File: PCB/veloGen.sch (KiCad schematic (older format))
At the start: 18 parts

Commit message: Got more specific about parts
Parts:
- D? (x4): value D_Schottky -> B5819WS
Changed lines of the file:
@@
 LIBS:valves
 LIBS:myStuff
+LIBS:veloGen-cache
 EELAYER 26 0
 EELAYER END
@@
 P 2000 1350
 F 0 "D?" V 2000 1429 50  0000 L CNN
-F 1 "D_Schottky" V 2045 1429 50  0001 L CNN
+F 1 "B5819WS" V 2045 1429 50  0001 L CNN
 F 2 "" H 2000 1350 50  0001 C CNN
 F 3 "" H 2000 1350 50  0001 C CNN
@@
 P 2600 1350
 F 0 "D?" V 2600 1429 50  0000 L CNN
-F 1 "D_Schottky" V 2645 1429 50  0001 L CNN
+F 1 "B5819WS" V 2645 1429 50  0001 L CNN
 F 2 "" H 2600 1350 50  0001 C CNN
 F 3 "" H 2600 1350 50  0001 C CNN
@@
 P 2000 2000
 F 0 "D?" V 2000 2079 50  0000 L CNN
-F 1 "D_Schottky" V 2045 2079 50  0001 L CNN
+F 1 "B5819WS" V 2045 2079 50  0001 L CNN
 F 2 "" H 2000 2000 50  0001 C CNN
 F 3 "" H 2000 2000 50  0001 C CNN
@@
 P 2600 2000
 F 0 "D?" V 2600 2079 50  0000 L CNN
-F 1 "D_Schottky" V 2645 2079 50  0001 L CNN
+F 1 "B5819WS" V 2645 2079 50  0001 L CNN
 F 2 "" H 2600 2000 50  0001 C CNN
 F 3 "" H 2600 2000 50  0001 C CNN

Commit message: Started the Schematic
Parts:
- removed Q?: FDS9934C, Housings_SOIC:SOIC-8_3.9x4.9mm_Pitch1.27mm, symbol FDS9934C
- removed Q?: BSS138, TO_SOT_Packages_SMD:SOT-23, symbol BSS138
- removed R?: R, symbol R
- removed U?: esp8266_esp-02, symbol esp8266_esp-02
- added C? (x5): 470n, symbol C
- added C? (x4): 47n, symbol C
- added D?: B5819WS, symbol D_Schottky
- added P?: TTL_232R_3V3, Pin_Headers:Pin_Header_Straight_1x06_Pitch2.54mm, symbol TTL_232R_3V3
- added Q?: STL6N3LLH6, myStuff:PowerFLAT_2x2, symbol STL6N3LLH6
- added R?: 47k, symbol R
- added R? (x4): R, symbol R
- added U?: LTC4440-5, TO_SOT_Packages_SMD:SOT-23-6_Handsoldering, symbol LTC4440
- added U? (x2): TS1101, TO_SOT_Packages_SMD:SOT-23-6_Handsoldering, symbol TS1101
- added U?: ESP-WROOM-32, myStuff:ESP-WROOM-32, symbol ESP-WROOM-32
- C?: value 1u -> 470n
- D?: value D_Schottky -> STPS3L40UF; footprint (none) -> Diodes_SMD:D_SMB_Standard
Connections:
- net labels added: +BATT, Ibatt, IbattSign, Igen, Vbatt, Vgen, buckPwm, speedPulse
- wire segments 45 -> 149
- no-connect marks 1 -> 2
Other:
- note added: "A minimalistic bluetooth bike computer\nand hub dynamo power manager"
- note added: "TODO:\n* Voltage divider values\n* Current Shunt values\n* ESP32 Pin assignment"
- moved on the sheet: C?, D?, J?, L?, R?, U?

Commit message: Refined the schematic
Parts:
- removed C? (x2): 10u, symbol C
- removed C? (x2): 470n, symbol C
- removed D?: STPS3L40UF, Diodes_SMD:D_SMB_Standard, symbol D_Schottky
- removed D?: B5819WS, symbol D_Schottky
- removed L?: L, symbol L
- removed Q?: STL6N3LLH6, myStuff:PowerFLAT_2x2, symbol STL6N3LLH6
- removed U?: LTC4440-5, TO_SOT_Packages_SMD:SOT-23-6_Handsoldering, symbol LTC4440
- added P?: CONN_01X04, symbol CONN_01X04
- added Q?: IRF7324, Housings_SOIC:SOIC-8_3.9x4.9mm_Pitch1.27mm, symbol IRF7324
- added Q?: 2N7002, TO_SOT_Packages_SMD:SOT-23, symbol 2N7002
- added R? (x2): 200R, symbol R
- added R? (x2): 4k7, symbol R
- added R?: 4.7Meg, symbol R
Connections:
- net labels added: extScl, extSda, vExtEnable
- wire segments 149 -> 102
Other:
- moved on the sheet: C?, U?

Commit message: Schematic one step closer
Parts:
- removed Q?: IRF7324, Housings_SOIC:SOIC-8_3.9x4.9mm_Pitch1.27mm, symbol IRF7324
- removed Q?: 2N7002, TO_SOT_Packages_SMD:SOT-23, symbol 2N7002
- added J1: CONN_01X02, Pin_Headers:Pin_Header_Straight_1x02_Pitch1.27mm, symbol CONN_01X02
- added Q1: STL4P3LLH6, myStuff:PowerFLAT_2x2, symbol STL4P3LLH6
- added Q2: BSS138_ok, TO_SOT_Packages_SMD:SOT-23, symbol BSS138_ok
- added R2: 470k, Resistors_SMD:R_0805, symbol R
- C1, C2, C3, C4, C5, C6, C7, C8: renamed from C?; footprint (none) -> Capacitors_SMD:C_0805
- D1, D2, D3, D4: renamed from D?; footprint (none) -> Diodes_SMD:D_SOD-323
- J2, J3: renamed from J?; footprint (none) -> Pin_Headers:Pin_Header_Straight_1x02_Pitch1.27mm
- P2: renamed from P?; footprint (none) -> Pin_Headers:Pin_Header_Straight_1x04_Pitch1.27mm
- R1, R10, R11, R12, R13, R3, R8, R9: renamed from R?; footprint (none) -> Resistors_SMD:R_0805
- R4: renamed from R?; value R -> 30k1; footprint (none) -> Resistors_SMD:R_0805
- R5: renamed from R?; value R -> 1k15; footprint (none) -> Resistors_SMD:R_0805
- R6: renamed from R?; value R -> 1M150; footprint (none) -> Resistors_SMD:R_0805
- R7: renamed from R?; value R -> 365k; footprint (none) -> Resistors_SMD:R_0805
- gave numbers to parts that had none: 5
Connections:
- net labels added: rstBtn
- wire segments 102 -> 114
- no-connect marks 2 -> 23
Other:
- note added: "30 V --> 1.1 V"
- note removed: "TODO:\n* Voltage divider values\n* Current Shunt values\n* ESP32 Pin assignment"
- moved on the sheet: C1, P1, U1

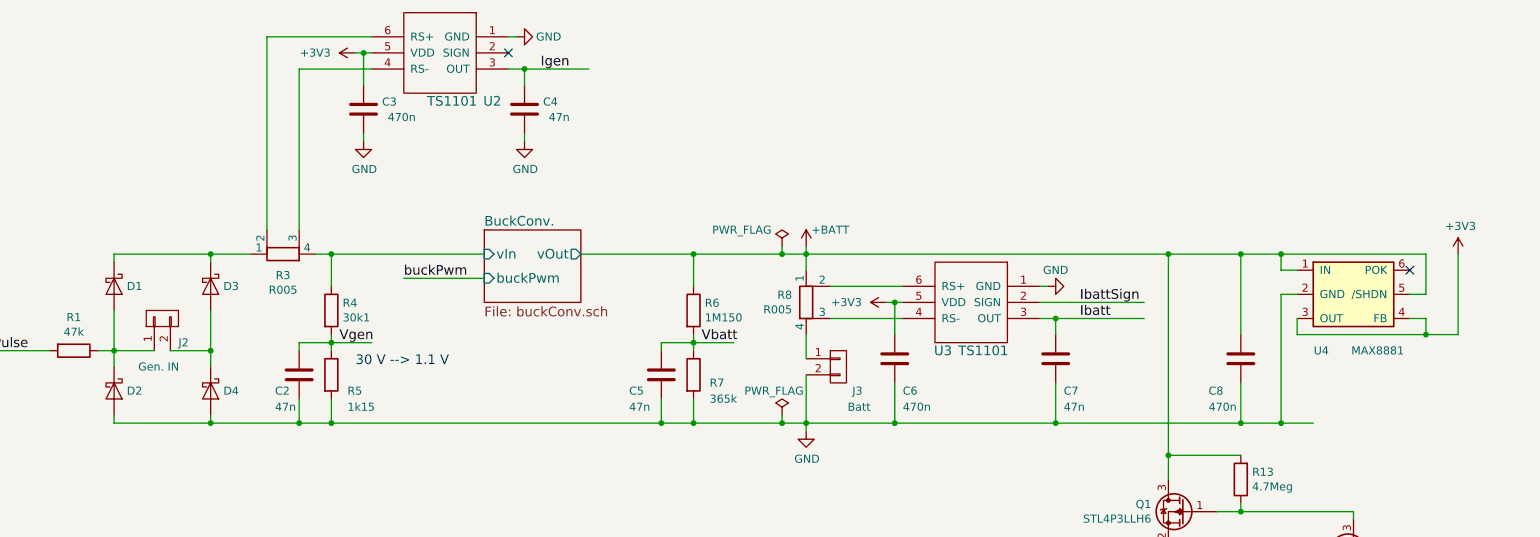
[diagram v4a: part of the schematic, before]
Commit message: Moved around some components a bit
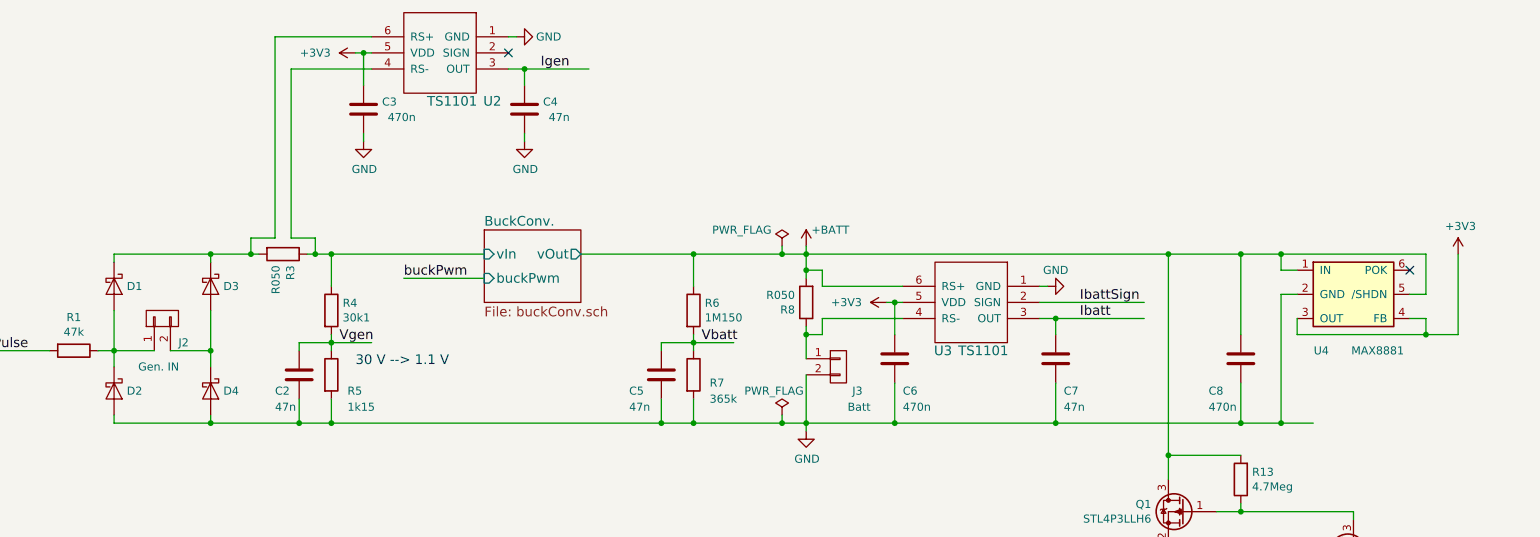
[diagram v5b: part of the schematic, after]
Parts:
- removed R3, R8: R005, Resistors_SMD:R_0805, symbol R_Shunt
- added R3, R8: R050, Resistors_SMD:R_0805, symbol R
- J1, J2, J3: footprint Pin_Headers:Pin_Header_Straight_1x02_Pitch1.27mm -> Pin_Headers:Pin_Header_Straight_1x02_Pitch2.54mm
- P2: footprint Pin_Headers:Pin_Header_Straight_1x04_Pitch1.27mm -> Pin_Headers:Pin_Header_Straight_1x04_Pitch2.54mm
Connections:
- wire segments 114 -> 121
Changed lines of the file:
@@
 F 0 "J2" V 2400 2800 50  0000 R CNN
 F 1 "Gen. IN" V 2250 3050 50  0000 R CNN
-F 2 "Pin_Headers:Pin_Header_Straight_1x02_Pitch1.27mm" H 2550 2900 50  0001 C CNN
+F 2 "Pin_Headers:Pin_Header_Straight_1x02_Pitch2.54mm" H 2550 2900 50  0001 C CNN
 F 3 "" H 2550 2900 50  0001 C CNN
 	1    2550 2900
@@
 $EndComp
 $Comp
-L R_Shunt R3
-U 1 1 58CDA790
-P 3300 2500
-F 0 "R3" V 3168 2500 50  0000 C CNN
-F 1 "R005" V 3077 2500 50  0000 C CNN
-F 2 "Resistors_SMD:R_0805" V 3230 2500 50  0001 C CNN
-F 3 "" H 3300 2500 50  0001 C CNN
-	1    3300 2500
-	0    -1   -1   0
-$EndComp
-$Comp
 L CONN_01X02 J3
 U 1 1 58CDC990
@@
 F 0 "J3" H 6900 3050 50  0000 R CNN
 F 1 "Batt" H 6950 2950 50  0000 R CNN
-F 2 "Pin_Headers:Pin_Header_Straight_1x02_Pitch1.27mm" H 6750 3200 50  0001 C CNN
+F 2 "Pin_Headers:Pin_Header_Straight_1x02_Pitch2.54mm" H 6750 3200 50  0001 C CNN
 F 3 "" H 6750 3200 50  0001 C CNN
 	1    6750 3200
-	1    0    0    -1
-$EndComp
-$Comp
-L R_Shunt R8
-U 1 1 58CDCDCD
-P 6550 2800
-F 0 "R8" H 6462 2846 50  0000 R CNN
-F 1 "R005" H 6462 2755 50  0000 R CNN
-F 2 "Resistors_SMD:R_0805" V 6480 2800 50  0001 C CNN
-F 3 "" H 6550 2800 50  0001 C CNN
-	1    6550 2800
 	1    0    0    -1
 $EndComp
@@
 F 0 "P2" H 8650 5100 50  0000 C CNN
 F 1 "CONN_01X04" H 8600 5000 50  0000 C CNN
-F 2 "Pin_Headers:Pin_Header_Straight_1x04_Pitch1.27mm" H 8500 5300 50  0001 C CNN
+F 2 "Pin_Headers:Pin_Header_Straight_1x04_Pitch2.54mm" H 8500 5300 50  0001 C CNN
 F 3 "" H 8500 5300 50  0000 C CNN
 	1    8500 5300
@@
 F 0 "J1" H 1419 5075 50  0000 C CNN
 F 1 "CONN_01X02" H 1419 5166 50  0000 C CNN
-F 2 "Pin_Headers:Pin_Header_Straight_1x02_Pitch1.27mm" H 1500 5350 50  0001 C CNN
+F 2 "Pin_Headers:Pin_Header_Straight_1x02_Pitch2.54mm" H 1500 5350 50  0001 C CNN
 F 3 "" H 1500 5350 50  0001 C CNN
 	1    1500 5350
@@
 Connection ~ 6400 3550
 Wire Wire Line
-	6400 3500 6400 3550
+	6400 3550 6400 3500
 Connection ~ 6400 2500
 Wire Wire Line
@@
 	8750 5350 8700 5350
 Wire Wire Line
-	2250 2500 3100 2500
+	2250 2500 3150 2500
 Wire Wire Line
 	4900 5800 5550 5800
@@
 	8800 2500 8800 3900
 Wire Wire Line
-	10400 2750 10400 2500
+	10400 2500 10400 2750
 Connection ~ 9500 2500
 Wire Wire Line
@@
 	9600 2600 9500 2600
 Wire Wire Line
-	9500 2750 9500 3550
-Wire Wire Line
-	9600 2750 9500 2750
+	9500 3550 9500 2750
+Wire Wire Line
+	9500 2750 9600 2750
 Wire Wire Line
 	9600 2900 9600 3000
 Connection ~ 9250 3550
 Wire Wire Line
-	9250 3300 9250 3550
+	9250 3550 9250 3300
 Connection ~ 9500 3550
 Wire Wire Line
-	3500 2500 4550 2500
+	3450 2500 4550 2500
 Wire Wire Line
 	4050 2650 4550 2650
@@
 	8100 3000 8100 2900
 Wire Wire Line
-	3850 1350 3400 1350
-Wire Wire Line
-	3200 1150 3850 1150
+	3850 1350 3350 1350
+Wire Wire Line
+	3250 1150 3850 1150
 Connection ~ 4800 1350
 Wire Wire Line
@@
 Connection ~ 2950 5100
 Wire Wire Line
-	2950 5100 2950 5100
+	2900 5100 3000 5100
 Connection ~ 2550 5100
 Wire Wire Line
@@
 Wire Wire Line
 	2550 5200 3000 5200
-Wire Wire Line
-	2900 5100 3000 5100
 Wire Wire Line
 	2500 5100 2600 5100
 Connection ~ 5650 3550
 Wire Wire Line
-	5650 3400 5650 3550
+	5650 3550 5650 3400
 Connection ~ 5850 3550
 Wire Wire Line
-	5850 3400 5850 3550
+	5850 3550 5850 3400
 Connection ~ 5850 2500
 Wire Wire Line
@@
 Connection ~ 8100 3550
 Wire Wire Line
-	8100 3300 8100 3550
-Wire Wire Line
-	3200 2350 3200 1150
-Wire Wire Line
-	3400 1350 3400 2350
+	8100 3550 8100 3300
+Wire Wire Line
+	3250 1150 3250 2400
+Wire Wire Line
+	3350 1350 3350 2400
 Wire Wire Line
 	3800 1800 3800 1750
@@
 	7050 2800 7150 2800
 Wire Wire Line
-	7150 2900 6700 2900
-Wire Wire Line
-	7150 2700 6700 2700
+	6650 2900 7150 2900
+Wire Wire Line
+	6650 2700 7150 2700
 Wire Wire Line
 	9600 3000 10600 3000
@@
 	9250 3000 9250 2500
 Wire Wire Line
-	10300 2750 10400 2750
+	10400 2750 10300 2750
 Connection ~ 6550 3550
 Connection ~ 6550 2500
 Wire Wire Line
-	6550 2450 6550 2600
-Wire Wire Line
-	6550 3000 6550 3150
+	6550 2450 6550 2650
+Wire Wire Line
+	6550 2950 6550 3150
 Wire Wire Line
 	6550 3250 6550 3600
 Wire Wire Line
-	10400 2500 5150 2500
+	5150 2500 10400 2500
 Connection ~ 2850 3550
 Connection ~ 2850 2500
@@
 	1    0    0    -1
 $EndComp
+$Comp
+L R R3
+U 1 1 58D38E14
+P 3300 2500
+F 0 "R3" H 3370 2546 50  0000 L CNN
+F 1 "R050" H 3370 2455 50  0000 L CNN
+F 2 "Resistors_SMD:R_0805" V 3230 2500 50  0001 C CNN
+F 3 "" H 3300 2500 50  0001 C CNN
+	1    3300 2500
+	0    1    1    0
+$EndComp
+Wire Wire Line
+	3250 2400 3100 2400
+Wire Wire Line
+	3100 2400 3100 2500
+Connection ~ 3100 2500
+Wire Wire Line
+	3350 2400 3500 2400
+Wire Wire Line
+	3500 2400 3500 2500
+Connection ~ 3500 2500
+$Comp
+L R R8
+U 1 1 58D39C69
+P 6550 2800
+F 0 "R8" H 6620 2846 50  0000 L CNN
+F 1 "R050" H 6620 2755 50  0000 L CNN
+F 2 "Resistors_SMD:R_0805" V 6480 2800 50  0001 C CNN
+F 3 "" H 6550 2800 50  0001 C CNN
+	1    6550 2800
+	-1   0    0    1
+$EndComp
+Wire Wire Line
+	6650 2900 6650 3000
+Wire Wire Line
+	6650 3000 6550 3000
+Connection ~ 6550 3000
+Wire Wire Line
+	6650 2700 6650 2600
+Wire Wire Line
+	6650 2600 6550 2600
+Connection ~ 6550 2600
 $EndSCHEMATC

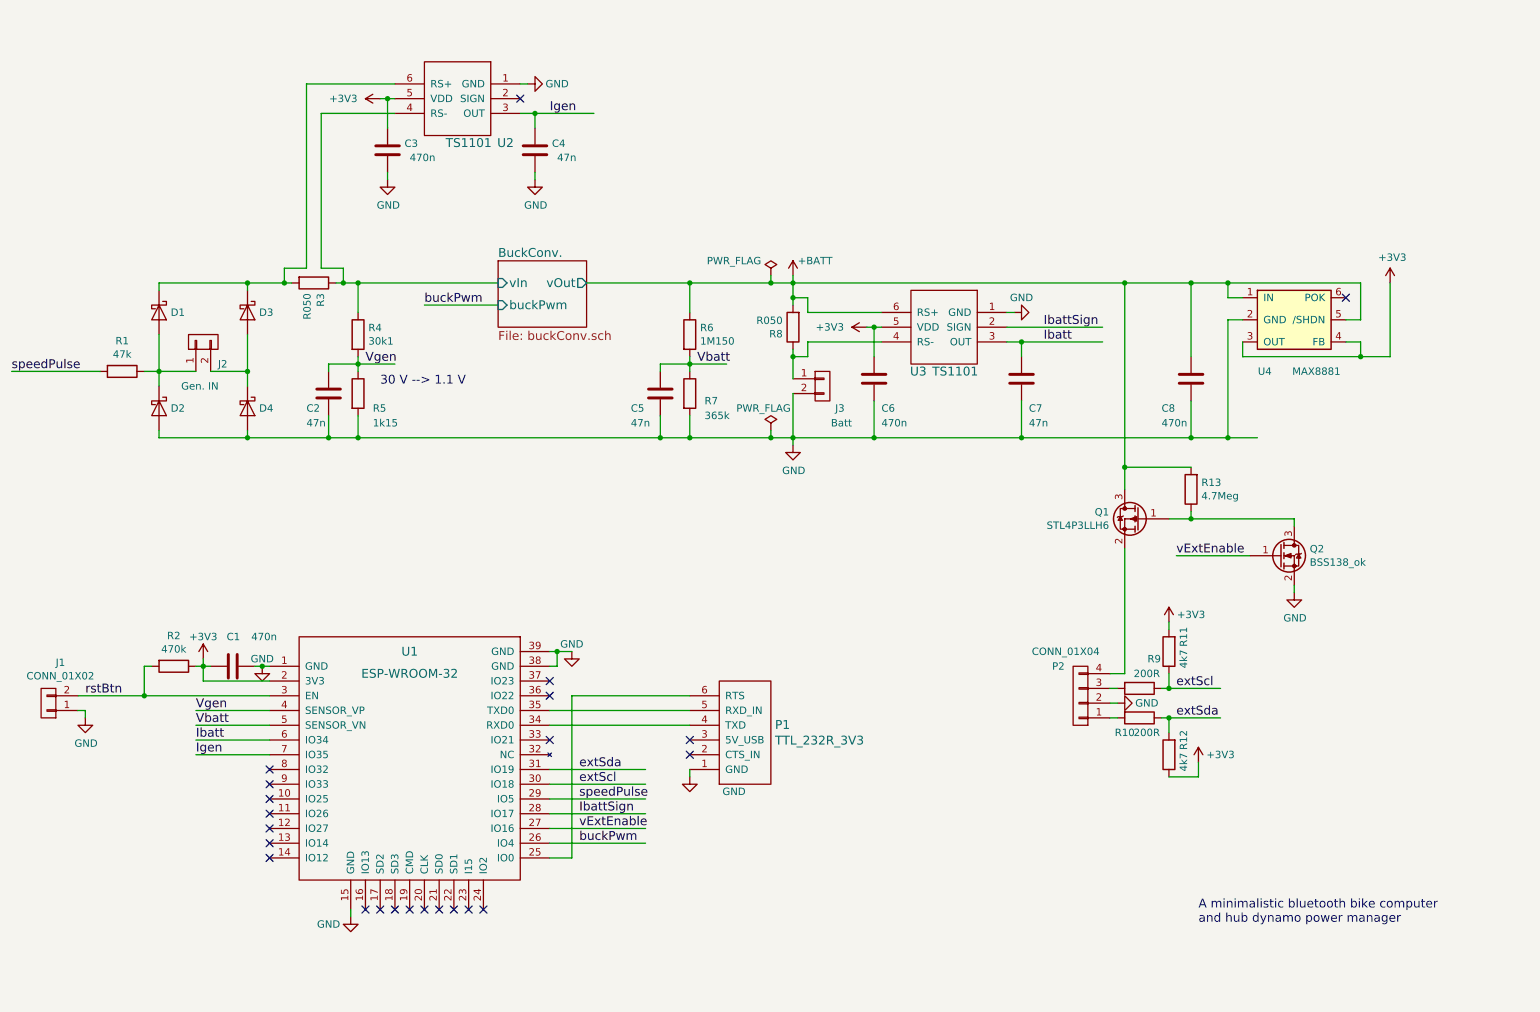
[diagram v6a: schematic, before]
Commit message: 80 MHz without WIFI: 26 mA
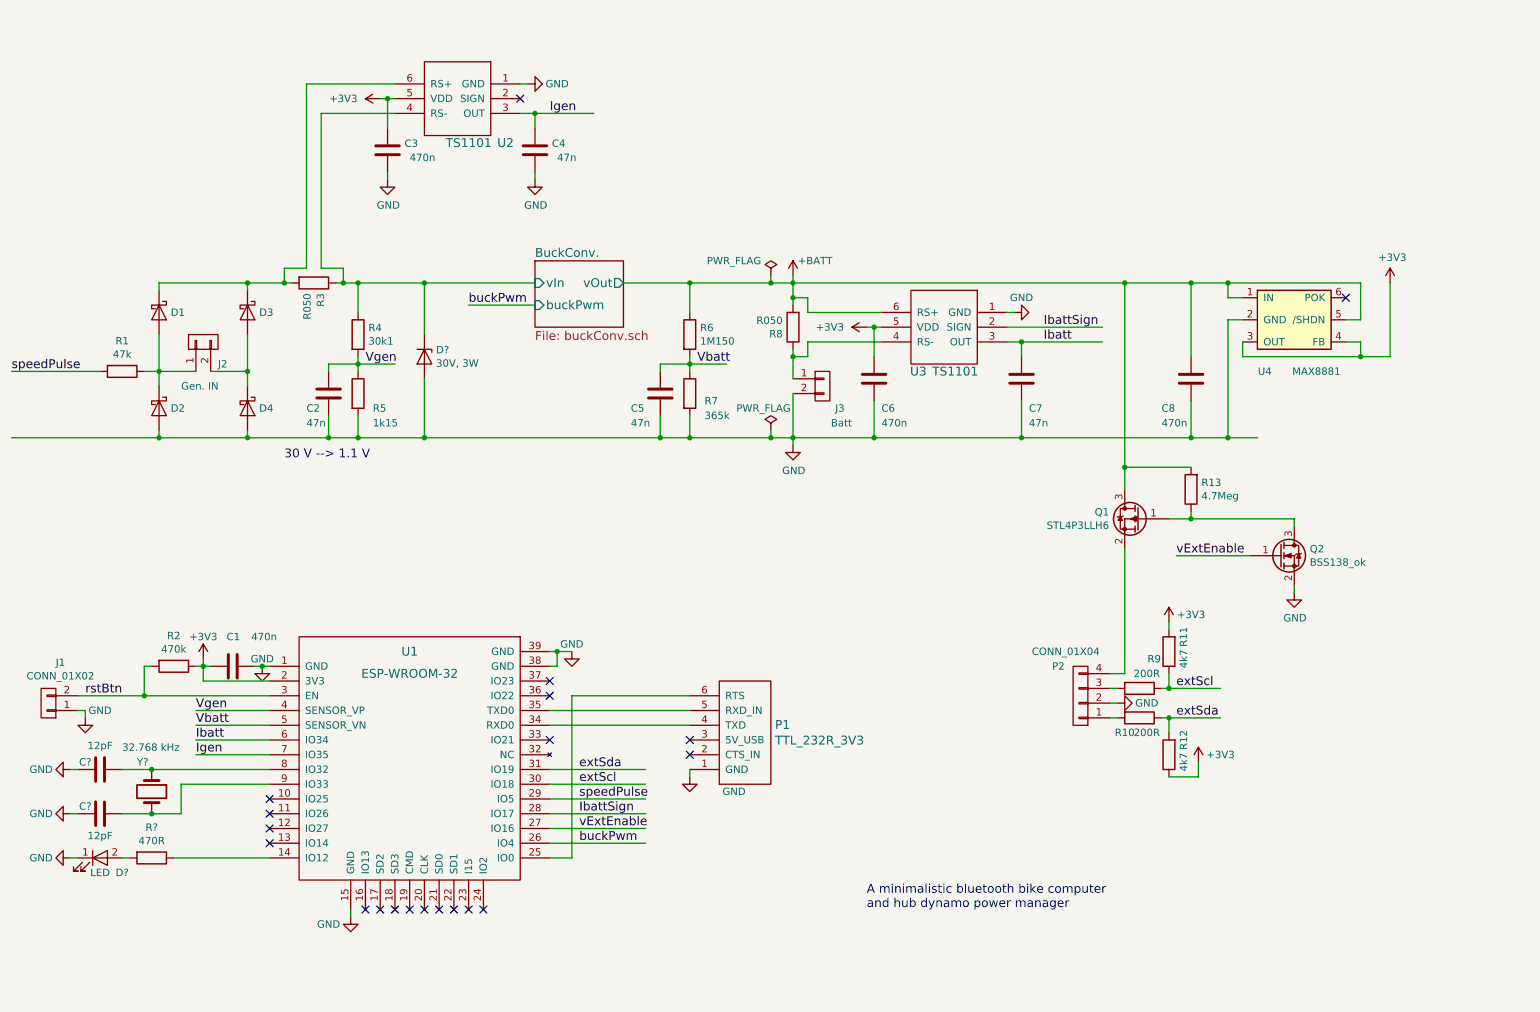
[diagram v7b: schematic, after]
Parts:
- added C? (x2): 12pF, symbol C
- added D?: LED, LEDs:LED_0805, symbol LED
- added D?: 30V, 3W, symbol D_Zener
- added R?: 470R, symbol R
- added Y?: 32.768 kHz, symbol Crystal
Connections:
- wire segments 121 -> 183
- no-connect marks 23 -> 20
